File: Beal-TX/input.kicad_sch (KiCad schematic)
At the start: 13 parts, among them J6 Screw_Terminal_01x06, U6 DRV8912QPWPRQ1

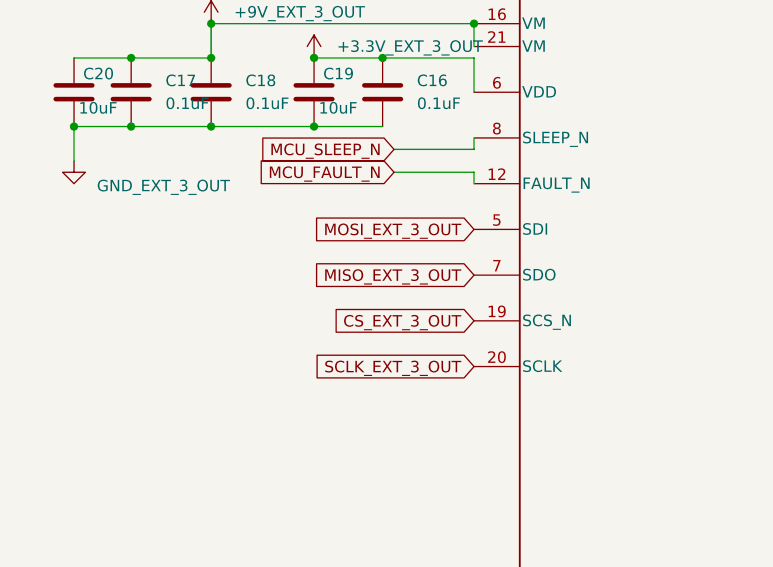
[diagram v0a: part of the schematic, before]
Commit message: Beal TX: Address some issues found during prototyping phase
Basically, the prototyping phase has highlighted some issues.
The major one is about the power delivered by an USB-C battery
is not enough to safely driver the valve.
The power after 9V decrease to about 5V, and the 5V from battery
fall to 2.0V.

One way for fixing it is using super capacitor.
This adds an extra cost to the BOM, and, I am not about its
duration regarding the operating conditions.

Because of the cost and the doubt about the longevity,
I would like to evaluate other solutions.
But, we also need to move forward so I made some changes to
power to make it more configurable so we could later try external
battery with a BMS, with different voltage with or without the booster.
By default we will have the super capacitor but we could slit main and
super capacitor board and plug a battery or any power source instead.

A minor change also introduced by this commit is adding testpoints.
Since the hardware an the software is not yet done, testpoints will
be very useful for debugging.

Signed-off-by: Alexandre Bailon <abailon@baylibre.com>
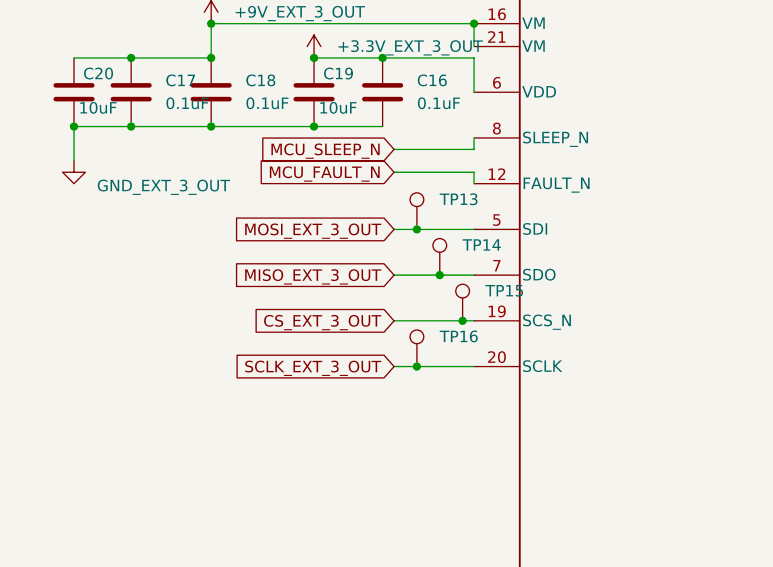
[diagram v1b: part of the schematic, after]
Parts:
- added TP13, TP14, TP15, TP16: TestPoint, TestPoint:TestPoint_Pad_D1.0mm, symbol Connector:TestPoint
- R5: MPN (none) -> 470 0402
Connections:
- net CS_EXT_3_OUT: now also TP15.1
- net MISO_EXT_3_OUT: now also TP14.1
- net MOSI_EXT_3_OUT: now also TP13.1
- net SCLK_EXT_3_OUT: now also TP16.1

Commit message: Beal-TX: Remove changes previoulsy done regarding done regarding battery tests
I made some measurement on comptitor product and finaly,
the signal to control the valve is not that bad.
I have decided to just add a capacitor and to remove all the
tests features added by previous commit.

This also tries to address some potential issues and does some
improvements such as increasing traces for VBUS and +9V.

Signed-off-by: Alexandre Bailon <abailon@baylibre.com>
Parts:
- added C11, C8: 8.2mF, Capacitor_THT:CP_Radial_D25.0mm_P10.00mm_SnapIn, symbol Device:C_Polarized
- added D10, D11, D2, D5, D8, D9: ESD9X12ST5G, Diode_SMD:D_SOD-923, symbol Pandora:ESD9X12ST5G
- added R14: 10K, Resistor_SMD:R_0402_1005Metric, symbol Device:R
- added R16: 30, Resistor_SMD:R_2512_6332Metric, symbol Device:R
- C20: footprint Resistor_SMD:R_1206_3216Metric -> Capacitor_SMD:C_1206_3216Metric
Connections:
- net +3.3V: now also R14.1
- net +9V: now also R16.1; no longer C17.1, C18.1, C20.1, U6.16 (VM), U6.21 (VM)
- net GND: now also C11.2, C8.2, D10.2 (A), D11.2 (A), D2.2 (A), D5.2 (A), D8.2 (A), D9.2 (A)
- net MCU_FAULT_N: now also R14.2
- net OUTPUT1_N: now also D10.1 (K)
- net OUTPUT1_P: now also D11.1 (K)
- net OUTPUT2_N: now also D8.1 (K)
- net OUTPUT2_P: now also D9.1 (K)
- net OUTPUT3_N: now also D2.1 (K)
- net OUTPUT3_P: now also D5.1 (K)
- new net +9V_VM: C11.1, C17.1, C18.1, C20.1, C8.1, R16.2, U6.16 (VM), U6.21 (VM)
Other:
- moved on the sheet: J6
